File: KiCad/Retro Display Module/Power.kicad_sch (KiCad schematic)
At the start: 18 parts, among them J18 Conn_01x02_Pin, J20 Conn_01x02_Pin, J22 Conn_01x02_Pin, U5 TPS5430DDAR, U6 XC6206P332MR

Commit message: Updated USB PD and Driver LED circuit
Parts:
- TP5, TP6, TP7: footprint TestPoint:TestPoint_Pad_2.0x2.0mm -> Library:TestPoint_THTPad_2.0x2.0mm_Drill1.0mm
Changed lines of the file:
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@@
         )
         (path "/046eef48-6d3f-4288-a12a-fc20b7e12e30/b83b8eb2-0716-4cf7-9ac5-6883d8975061"
-          (reference "#PWR09") (unit 1)
+          (reference "#PWR010") (unit 1)
         )
       )
@@
       (effects (font (size 1.27 1.27)) (justify left))
     )
-    (property "Footprint" "TestPoint:TestPoint_Pad_2.0x2.0mm" (at 207.01 85.09 0)
+    (property "Footprint" "Library:TestPoint_THTPad_2.0x2.0mm_Drill1.0mm" (at 207.01 85.09 0)
       (effects (font (size 1.27 1.27)) hide)
     )
@@
         )
         (path "/046eef48-6d3f-4288-a12a-fc20b7e12e30/b83b8eb2-0716-4cf7-9ac5-6883d8975061"
-          (reference "#PWR011") (unit 1)
+          (reference "#PWR012") (unit 1)
         )
       )
@@
         )
         (path "/046eef48-6d3f-4288-a12a-fc20b7e12e30/b83b8eb2-0716-4cf7-9ac5-6883d8975061"
-          (reference "#PWR012") (unit 1)
+          (reference "#PWR013") (unit 1)
         )
       )
@@
         )
         (path "/046eef48-6d3f-4288-a12a-fc20b7e12e30/b83b8eb2-0716-4cf7-9ac5-6883d8975061"
-          (reference "#PWR013") (unit 1)
+          (reference "#PWR014") (unit 1)
         )
       )
@@
       (effects (font (size 1.27 1.27)) (justify left))
     )
-    (property "Footprint" "TestPoint:TestPoint_Pad_2.0x2.0mm" (at 152.4 102.87 0)
+    (property "Footprint" "Library:TestPoint_THTPad_2.0x2.0mm_Drill1.0mm" (at 152.4 102.87 0)
       (effects (font (size 1.27 1.27)) hide)
     )
@@
         )
         (path "/046eef48-6d3f-4288-a12a-fc20b7e12e30/b83b8eb2-0716-4cf7-9ac5-6883d8975061"
-          (reference "#PWR014") (unit 1)
+          (reference "#PWR015") (unit 1)
         )
       )
@@
         )
         (path "/046eef48-6d3f-4288-a12a-fc20b7e12e30/b83b8eb2-0716-4cf7-9ac5-6883d8975061"
-          (reference "#PWR015") (unit 1)
+          (reference "#PWR016") (unit 1)
         )
       )
@@
       (effects (font (size 1.27 1.27)) (justify left))
     )
-    (property "Footprint" "TestPoint:TestPoint_Pad_2.0x2.0mm" (at 87.63 92.71 0)
+    (property "Footprint" "Library:TestPoint_THTPad_2.0x2.0mm_Drill1.0mm" (at 87.63 92.71 0)
       (effects (font (size 1.27 1.27)) hide)
     )
@@
         )
         (path "/046eef48-6d3f-4288-a12a-fc20b7e12e30/b83b8eb2-0716-4cf7-9ac5-6883d8975061"
-          (reference "#PWR010") (unit 1)
-        )
-      )
+          (reference "#PWR011") (unit 1)
+        )
+      )

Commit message: Begin STM32 Programming
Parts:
- J18, J20, J22: now left out of the parts list
- TP5, TP6, TP7: now not fitted; now left out of the parts list
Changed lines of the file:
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@@
   )
   (symbol (lib_id "Connector:TestPoint") (at 201.93 85.09 0) (unit 1)
-    (in_bom yes) (on_board yes) (dnp no) (fields_autoplaced)
+    (in_bom no) (on_board yes) (dnp yes) (fields_autoplaced)
     (property "Reference" "TP7" (at 203.327 81.1443 0)
       (effects (font (size 1.27 1.27)) (justify left))
@@
   )
   (symbol (lib_id "Connector:Conn_01x02_Pin") (at 107.95 101.6 0) (mirror y) (unit 1)
-    (in_bom yes) (on_board yes) (dnp yes)
+    (in_bom no) (on_board yes) (dnp yes)
     (property "Reference" "J18" (at 111.76 104.14 0)
       (effects (font (size 1.27 1.27)))
@@
   )
   (symbol (lib_id "Connector:Conn_01x02_Pin") (at 72.39 87.63 270) (unit 1)
-    (in_bom yes) (on_board yes) (dnp yes)
+    (in_bom no) (on_board yes) (dnp yes)
     (property "Reference" "J22" (at 66.04 86.36 90)
       (effects (font (size 1.27 1.27)))
@@
   )
   (symbol (lib_id "Connector:TestPoint") (at 147.32 102.87 0) (mirror x) (unit 1)
-    (in_bom yes) (on_board yes) (dnp no)
+    (in_bom no) (on_board yes) (dnp yes)
     (property "Reference" "TP5" (at 148.717 106.8157 0)
       (effects (font (size 1.27 1.27)) (justify left))
@@
   )
   (symbol (lib_id "Connector:TestPoint") (at 82.55 92.71 0) (unit 1)
-    (in_bom yes) (on_board yes) (dnp no)
+    (in_bom no) (on_board yes) (dnp yes)
     (property "Reference" "TP6" (at 83.947 88.7643 0)
       (effects (font (size 1.27 1.27)) (justify left))
@@
   )
   (symbol (lib_id "Connector:Conn_01x02_Pin") (at 172.72 82.55 90) (mirror x) (unit 1)
-    (in_bom yes) (on_board yes) (dnp yes)
+    (in_bom no) (on_board yes) (dnp yes)
     (property "Reference" "J20" (at 175.26 78.74 0)
       (effects (font (size 1.27 1.27)))

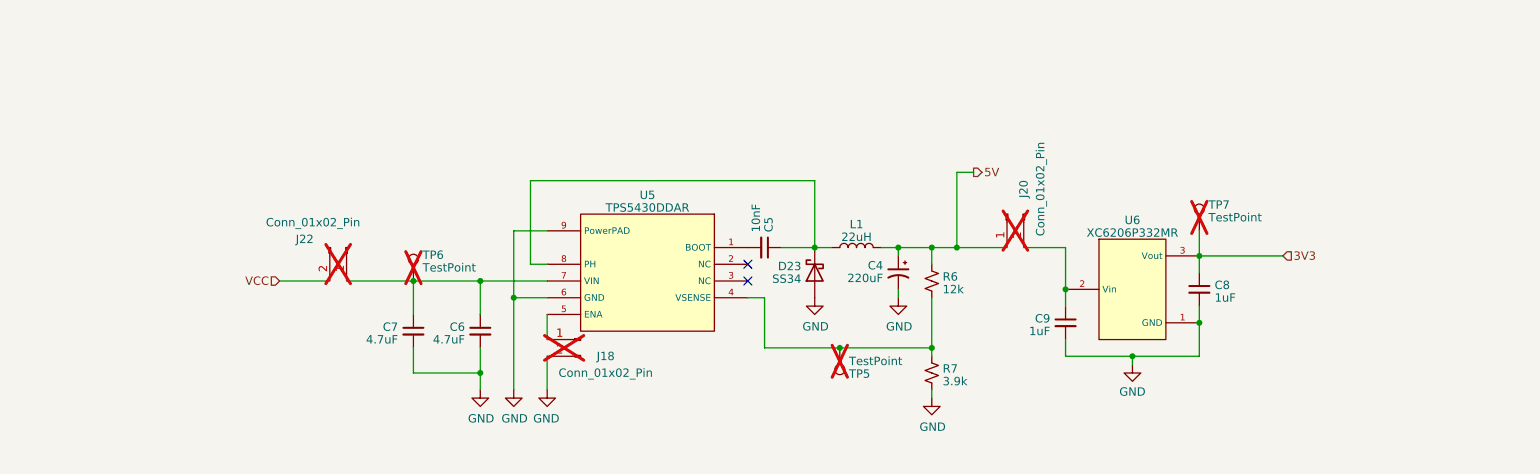
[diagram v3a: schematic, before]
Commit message: Updated Schematics and Added Reverse polarity protection
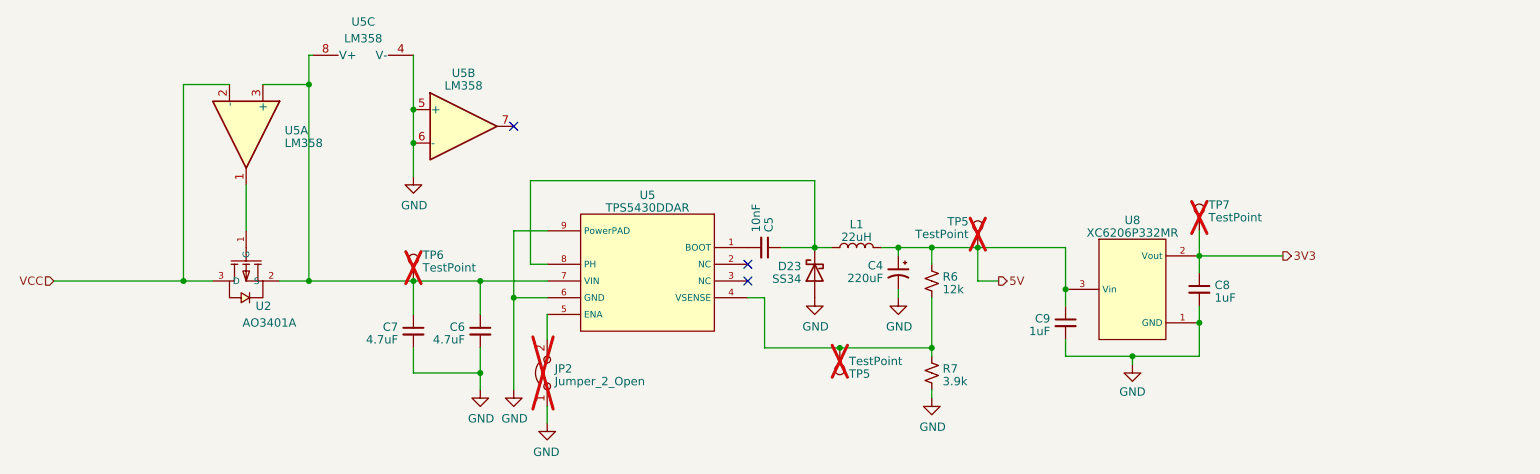
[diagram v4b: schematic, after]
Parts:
- removed J18, J20, J22: Conn_01x02_Pin, Connector_PinHeader_2.54mm:PinHeader_1x02_P2.54mm_Vertical, symbol Connector:Conn_01x02_Pin
- removed U6: XC6206P332MR, Library:XC6206, symbol EEE4022S:XC6206P332MR
- added JP2: Jumper_2_Open, Jumper:SolderJumper-2_P1.3mm_Open_RoundedPad1.0x1.5mm, symbol Jumper:Jumper_2_Open
- added TP5: TestPoint, Library:TestPoint_THTPad_2.0x2.0mm_Drill1.0mm, symbol Connector:TestPoint
- added U2: AO3401A, Library:SOT-23_L2.9-W1.3-P1.90-LS2.4-BR, symbol EEE4022S:AO3401A
- added unit 2 of U5
- added unit 3 of U5
- added U8: XC6206P332MR, Library:SOT-23-3_L2.9-W1.3-P1.90-LS2.4-BR, symbol EEE4022S:XC6206P332MR
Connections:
- net 3V3: now also U8.2 (Vout)
- net 5V: now also C9.1, TP5.1, U8.3 (Vin)
- net GND: now also JP2.1 (A), U5.4 (V-), U5.5 (+), U5.6 (-), U8.1 (GND)
- net VCC: now also U2.3 (D), U5.2 (-)
- net at C6.1, C7.1, TP6.1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: now also U2.2 (S), U5.3 (+), U5.8 (V+)
- net at U5.5 (ENA): now also JP2.2 (B)
- new net: U2.1 (G), U5.1
- no-connect marks 2 -> 3

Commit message: Added reverse polarity protection
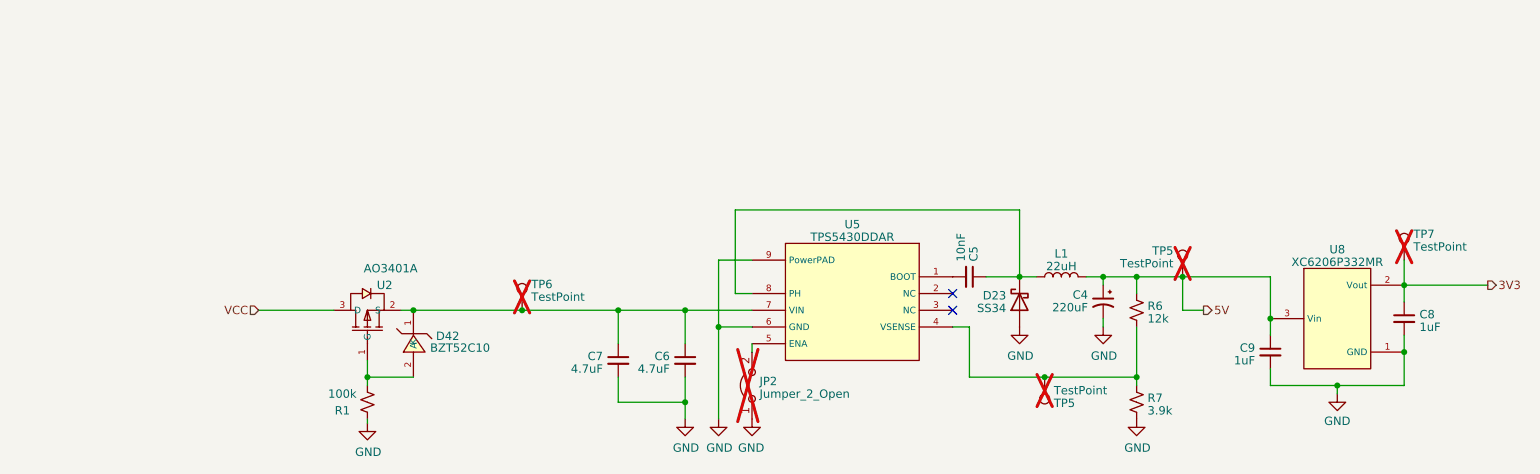
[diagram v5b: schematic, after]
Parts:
- removed unit 2 of U5
- removed unit 3 of U5
- added D42: BZT52C10, Library:SOD-123_L2.8-W1.8-LS3.7-RD BZT52C10, symbol EEE4022S:BZT52C10_C173431
- added R1: 100k, Library:R_0402_1005Metric_Pad0.72x0.64mm_HandSolder, symbol Device:R_Small_US
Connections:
- net GND: now also R1.2
- net at C6.1, C7.1, TP6.1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: now also D42.1 (K)
- net at U2.1 (G): now also D42.2 (A), R1.1
- no-connect marks 3 -> 2
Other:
- moved on the sheet: C4, C5, C6, C7, C8, C9, D23, JP2, L1, R6, R7, TP5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
